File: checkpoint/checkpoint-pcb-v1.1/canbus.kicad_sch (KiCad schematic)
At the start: 14 parts, among them J10 CAN_OUT, U2 SN65HVD1050D

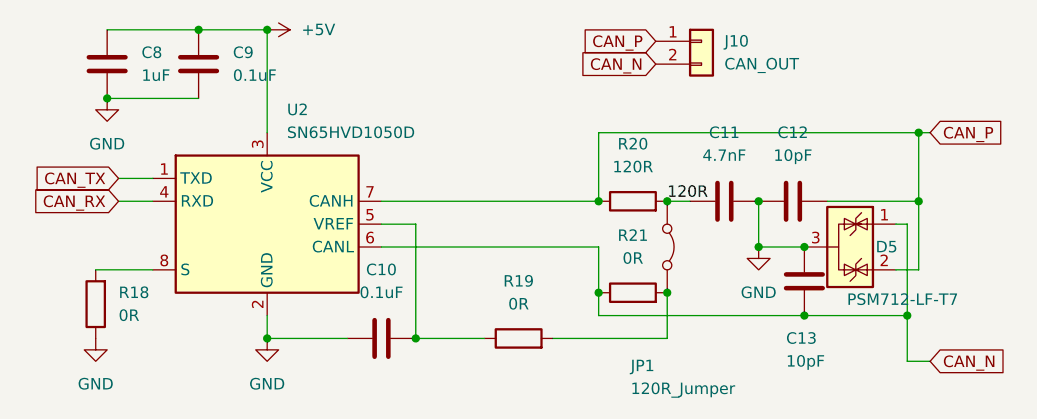
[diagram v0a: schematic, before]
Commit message: fix: swap can lines to match BTT convention
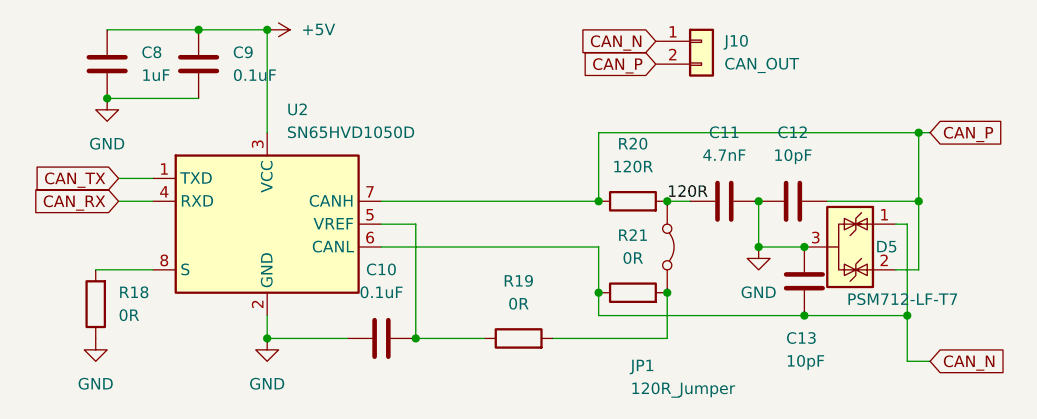
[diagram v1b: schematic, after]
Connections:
- net CAN_N: now also J10.1 (Pin_1); no longer J10.2 (Pin_2)
- net CAN_P: now also J10.2 (Pin_2); no longer J10.1 (Pin_1)
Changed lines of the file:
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@@
 	(global_label "CAN_P"
 		(shape input)
-		(at 156.21 77.47 180)
+		(at 156.21 80.01 180)
 		(fields_autoplaced yes)
 		(effects
@@
 		)
 		(property "Intersheetrefs" "${INTERSHEET_REFS}"
-			(at 147.2981 77.47 0)
+			(at 147.2981 80.01 0)
 			(effects
 				(font
@@
 	(global_label "CAN_N"
 		(shape input)
-		(at 156.21 80.01 180)
+		(at 156.21 77.47 180)
 		(fields_autoplaced yes)
 		(effects
@@
 		)
 		(property "Intersheetrefs" "${INTERSHEET_REFS}"
-			(at 147.2376 80.01 0)
+			(at 147.2376 77.47 0)
 			(effects
 				(font

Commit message: chore: update component rotation
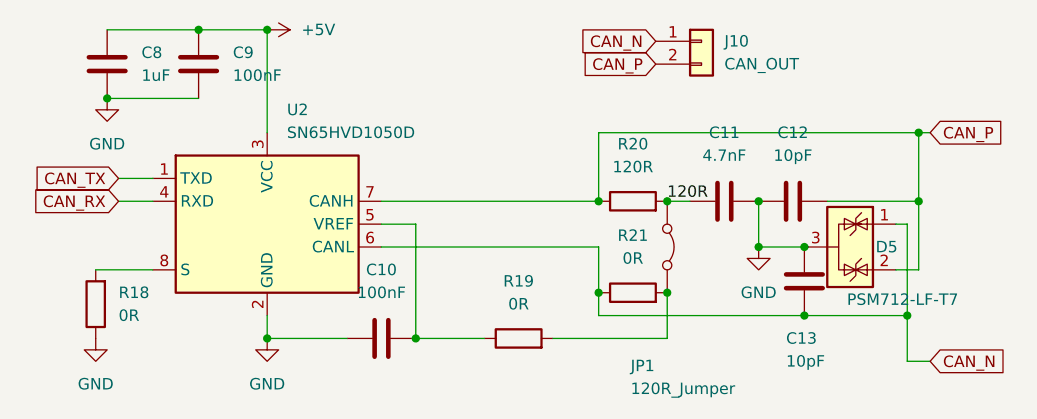
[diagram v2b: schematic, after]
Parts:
- C10, C9: value 0.1uF -> 100nF
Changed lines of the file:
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@@
 			)
 		)
-		(property "Value" "0.1uF"
+		(property "Value" "100nF"
 			(at 109.22 81.2799 0)
 			(effects
@@
 			)
 		)
-		(property "Value" "0.1uF"
+		(property "Value" "100nF"
 			(at 125.73 105.41 90)
 			(effects
